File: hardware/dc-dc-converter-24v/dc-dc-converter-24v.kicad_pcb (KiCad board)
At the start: 4 copper layers, 100 x 100 mm, 56 parts, among them J1 12V, J2 24V, Q1 SQJA42EP, Q2 SQJA42EP, Q3 SQJA42EP, Q4 SQJA42EP, U1 LM5176

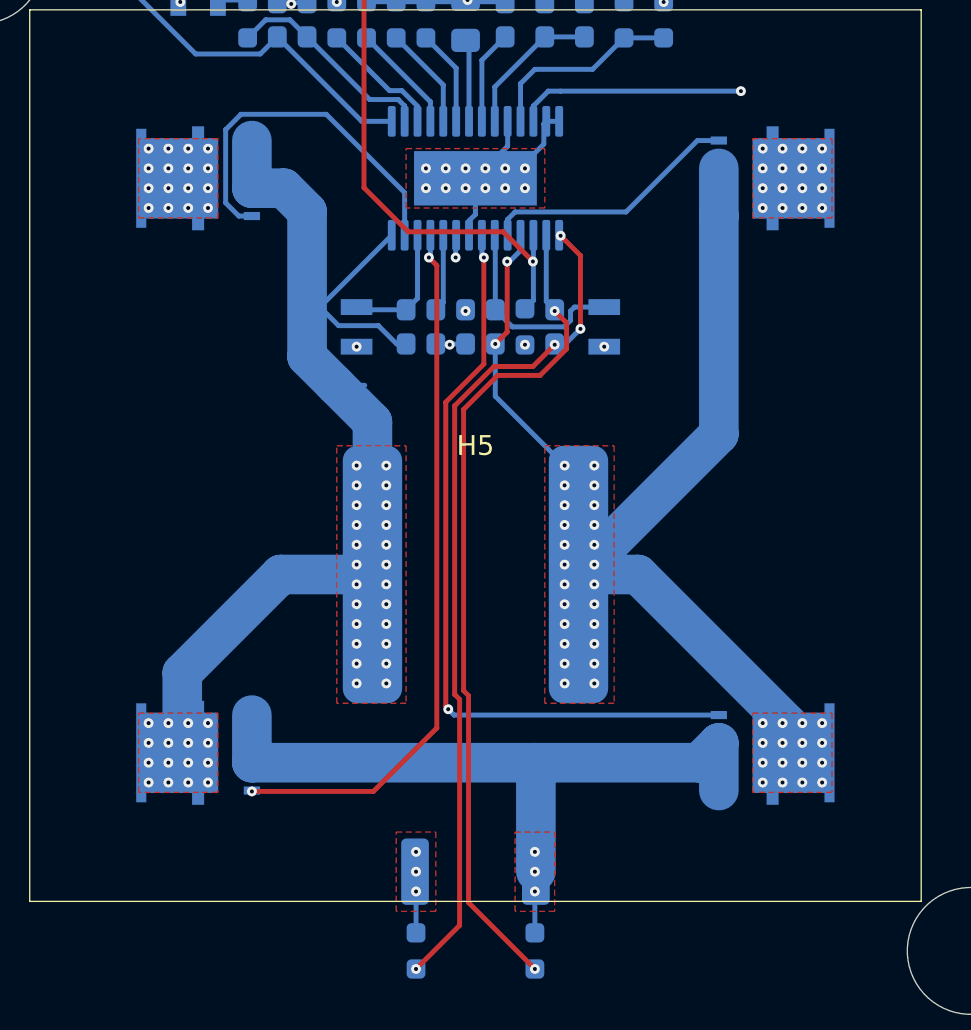
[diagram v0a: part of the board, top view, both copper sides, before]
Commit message: replace tracks in power path with zones
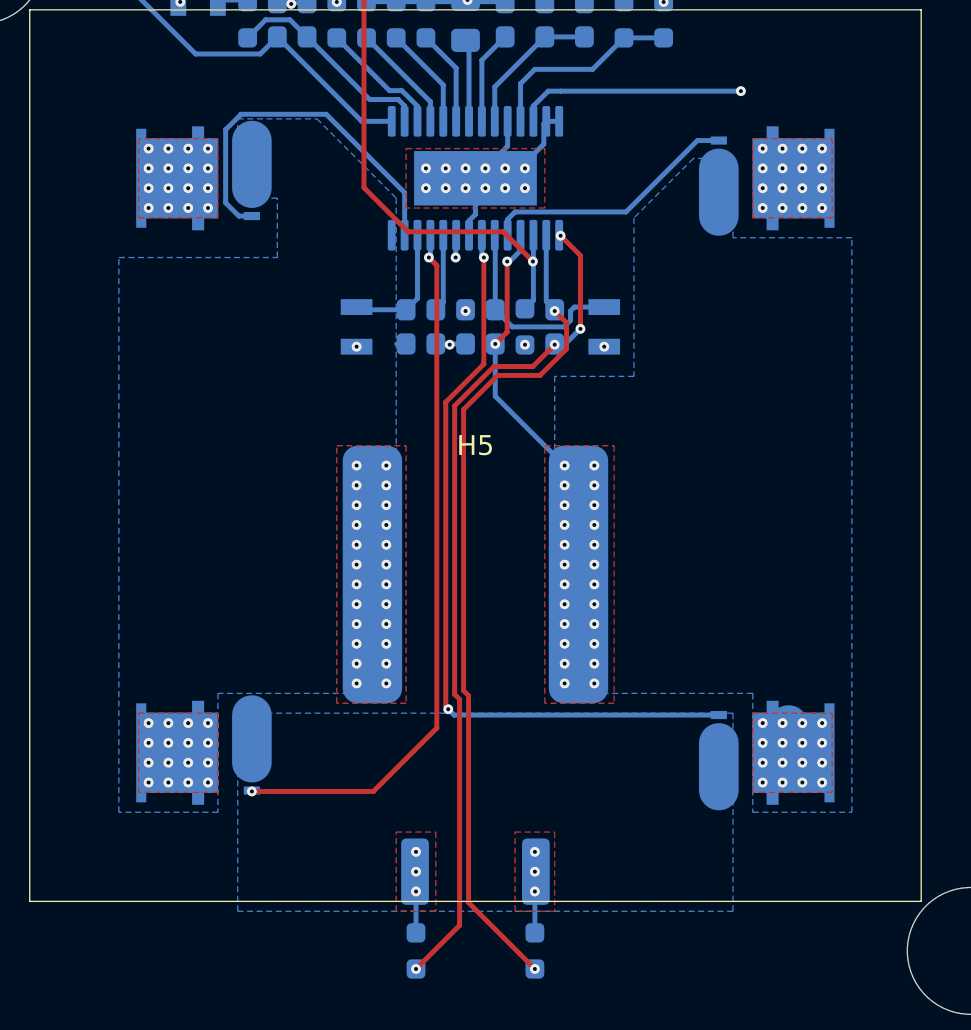
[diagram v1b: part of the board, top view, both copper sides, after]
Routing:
- net Net-(Q1-S): track 52.8 -> 2.88 mm
- net Net-(Q3-S): track 52.3 -> 17.5 mm
- net Net-(Q2-S): track 36.4 -> 6.90 mm
- added copper zone on B.Cu, net Net-(Q1-S)
- added copper zone on B.Cu, net Net-(Q2-S)
- added copper zone on B.Cu, net Net-(Q3-S)
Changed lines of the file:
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@@
-	)
-	(segment
-		(start 85.801 87.596)
-		(end 78.205 80)
-		(width 2)
-		(layer "B.Cu")
-		(net 11)
-	)
-	(segment
-		(start 82.285 72.915)
-		(end 75.2 80)
-		(width 2)
-		(layer "B.Cu")
-		(net 11)
-	)
-	(segment
-		(start 78.205 80)
-		(end 75.2 80)
-		(width 2)
-		(layer "B.Cu")
-		(net 11)
 	)
 	(segment
@@
 	)
 	(segment
-		(start 82.285 61.905)
-		(end 82.285 72.915)
-		(width 2)
-		(layer "B.Cu")
-		(net 11)
-	)
-	(segment
 		(start 85.801 89)
 		(end 85.801 87.596)
@@
 	)
 	(segment
-		(start 73.05 89.55)
-		(end 73.05 95)
-		(width 2)
-		(layer "B.Cu")
-		(net 21)
-	)
-	(segment
-		(start 58.715 89.5)
-		(end 73 89.5)
-		(width 2)
-		(layer "B.Cu")
-		(net 21)
-	)
-	(segment
 		(start 82.285 90.905)
 		(end 82.285 88.5)
@@
 	)
 	(segment
-		(start 81.285 89.5)
-		(end 82.285 88.5)
-		(width 2)
-		(layer "B.Cu")
-		(net 21)
-	)
-	(segment
 		(start 58.715 87.095)
 		(end 58.715 89.5)
@@
 		(net 21)
 	)
-	(segment
-		(start 73 89.5)
-		(end 73.05 89.55)
-		(width 2)
-		(layer "B.Cu")
-		(net 21)
-	)
-	(segment
-		(start 73 89.5)
-		(end 81.285 89.5)
-		(width 2)
-		(layer "B.Cu")
-		(net 21)
-	)
 	(via
 		(at 53.5 89.5)
@@
 		(drill 0.2)
 		(layers "F.Cu" "B.Cu")
-		(net 22)
-	)
-	(segment
-		(start 60.325 60.5)
-		(end 61.5 61.675)
-		(width 2)
-		(layer "B.Cu")
-		(net 22)
-	)
-	(segment
-		(start 64.4125 70.45)
-		(end 62.95 70.45)
-		(width 0.25)
-		(layer "B.Cu")
-		(net 22)
-	)
-	(segment
-		(start 63.0875 67.4375)
-		(end 62.15 66.5)
-		(width 0.25)
-		(layer "B.Cu")
-		(net 22)
-	)
-	(segment
-		(start 61.5 69)
-		(end 62.95 70.45)
-		(width 2)
-		(layer "B.Cu")
-		(net 22)
-	)
-	(segment
-		(start 58.715 60.5)
-		(end 60.325 60.5)
-		(width 2)
-		(layer "B.Cu")
-		(net 22)
-	)
-	(segment
-		(start 60.1685 80)
-		(end 64.8 80)
-		(width 2)
-		(layer "B.Cu")
-		(net 22)
-	)
-	(segment
-		(start 62.95 70.45)
-		(end 64.8 72.3)
-		(width 2)
-		(layer "B.Cu")
-		(net 22)
-	)
-	(segment
-		(start 61.5 61.675)
-		(end 61.5 69)
-		(width 2)
-		(layer "B.Cu")
-		(net 22)
-	)
-	(segment
-		(start 55.199 89)
-		(end 55.199 84.9695)
-		(width 2)
-		(layer "B.Cu")
-		(net 22)
-	)
-	(segment
-		(start 65.1 67.4375)
-		(end 63.0875 67.4375)
-		(width 0.25)
-		(layer "B.Cu")
 		(net 22)
 	)
@@
 		(end 66.025 68.3625)
 		(width 0.25)
-		(layer "B.Cu")
-		(net 22)
-	)
-	(segment
-		(start 55.199 84.9695)
-		(end 60.1685 80)
-		(width 2)
-		(layer "B.Cu")
-		(net 22)
-	)
-	(segment
-		(start 62.15 66.5)
-		(end 65.775 62.875)
-		(width 0.25)
-		(layer "B.Cu")
-		(net 22)
-	)
-	(segment
-		(start 66.025 68.3625)
-		(end 65.1 67.4375)
-		(width 0.25)
-		(layer "B.Cu")
-		(net 22)
-	)
-	(segment
-		(start 64.8 72.3)
-		(end 64.8 80)
-		(width 2)
 		(layer "B.Cu")
 		(net 22)
@@
 			)
 		)
+	)
+	(zone
+		(net 22)
+		(net_name "Net-(Q1-S)")
+		(layer "B.Cu")
+		(hatch edge 0.5)
+		(priority 13)
+		(connect_pads yes
+			(clearance 0.5)
+		)
+		(min_thickness 0.25)
+		(filled_areas_thickness no)
+		(fill yes
+			(thermal_gap 0.5)
+			(thermal_bridge_width 0.5)
+		)
+		(polygon
+			(pts
+				(xy 58 57) (xy 62 57) (xy 66 61) (xy 66 86) (xy 57 86) (xy 57 92) (xy 52 92) (xy 52 64) (xy 60 64)
+				(xy 60 61) (xy 58 61)
+			)
+		)
+	)
+	(zone
+		(net 11)
+		(net_name "Net-(Q3-S)")
+		(layer "B.Cu")
+		(hatch edge 0.5)
+		(priority 14)
+		(connect_pads yes
+			(clearance 0.5)
+		)
+		(min_thickness 0.25)
+		(filled_areas_thickness no)
+		(fill yes
+			(thermal_gap 0.5)
+			(thermal_bridge_width 0.5)
+		)
+		(polygon
+			(pts
+				(xy 83 59) (xy 81 59) (xy 78 62) (xy 78 70) (xy 74 70) (xy 74 86) (xy 84 86) (xy 84 92) (xy 89 92)
+				(xy 89 63) (xy 83 63)
+			)
+		)
+	)
+	(zone
+		(net 21)
+		(net_name "Net-(Q2-S)")
+		(layer "B.Cu")
+		(hatch edge 0.5)
+		(priority 15)
+		(connect_pads yes
+			(clearance 0.5)
+		)
+		(min_thickness 0.25)
+		(filled_areas_thickness no)
+		(fill yes
+			(thermal_gap 0.5)
+			(thermal_bridge_width 0.5)
+		)
+		(polygon
+			(pts
+				(xy 58 87) (xy 83 87) (xy 83 97) (xy 58 97)
+			)
+		)

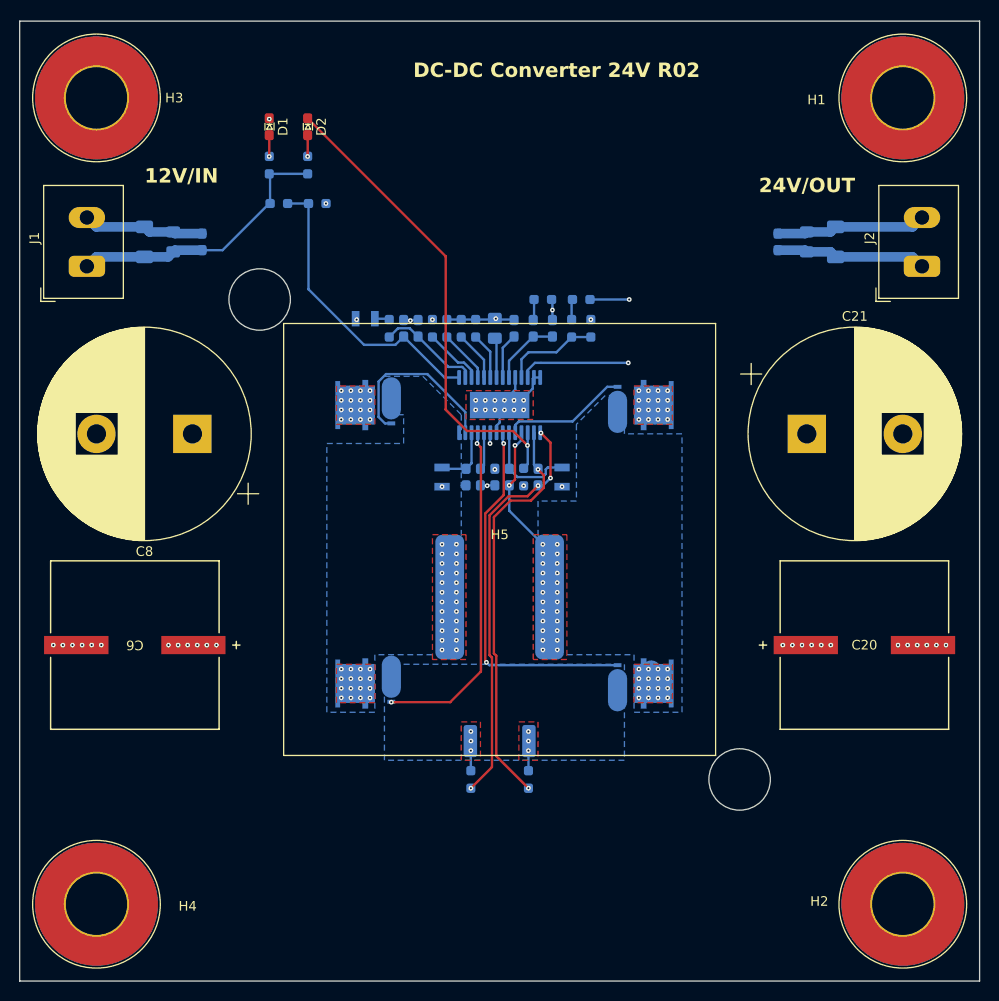
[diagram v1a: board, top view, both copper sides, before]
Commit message: improve layout of DC DC converter
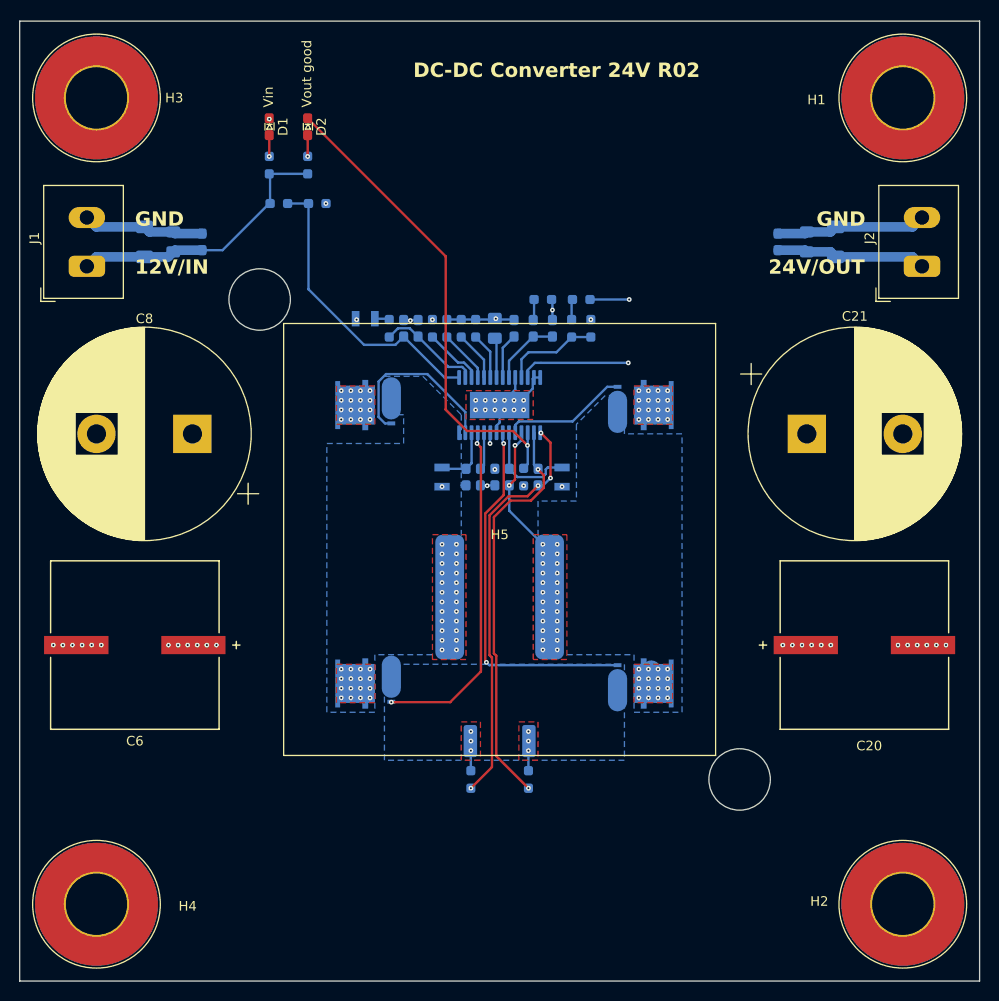
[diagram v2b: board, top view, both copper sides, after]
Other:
- board text added: "GND"
- board text added: "Vin"
- board text added: "Vout good"
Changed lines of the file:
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@@
 			(layer "F.SilkS")
 		)
+		(fp_circle
+			(center -25 -25)
+			(end -21 -22)
+			(stroke
+				(width 0.05)
+				(type default)
+			)
+			(fill none)
+			(layer "B.CrtYd")
+		)
+		(fp_circle
+			(center 25 25)
+			(end 29 27)
+			(stroke
+				(width 0.05)
+				(type default)
+			)
+			(fill none)
+			(layer "B.CrtYd")
+		)
 		(fp_line
 			(start -25 -32.5)
@@
 		(tags "CP Radial series Radial pin pitch 10.00mm  diameter 22mm Electrolytic Capacitor")
 		(property "Reference" "C8"
-			(at 5 -12.25 180)
+			(at 5 12 180)
 			(layer "F.SilkS")
 			(effects
@@
 		(tags "UCD1J471MNQ1MS ")
 		(property "Reference" "C20"
-			(at 0 0 0)
+			(at 0.5 10.5 0)
 			(unlocked yes)
 			(layer "F.SilkS")
@@
 			(pintype "passive")
 		)
+		(model "/home/benedikt/Development/electronics-library/3d-models/phoenix_1755736.stp"
+			(offset
+				(xyz -6.1 -3.9 0)
+			)
+			(scale
+				(xyz 1 1 1)
+			)
+			(rotate
+				(xyz 0 0 0)
+			)
+		)
 	)
 	(footprint "benediktibk:MountingHole_6.4mm_M6_Pad_TopBottom"
@@
 			(pintype "passive")
 		)
+		(model "/home/benedikt/Development/electronics-library/3d-models/phoenix_1755736.stp"
+			(offset
+				(xyz -6.1 -3.9 0)
+			)
+			(scale
+				(xyz 1 1 1)
+			)
+			(rotate
+				(xyz 0 0 0)
+			)
+		)
 	)
 	(footprint "benediktibk:MountingHole_6.4mm_M6_Pad_TopBottom"
@@
 		(tags "UCD1J471MNQ1MS ")
 		(property "Reference" "C6"
-			(at 0 0 180)
+			(at 0 -10 0)
 			(unlocked yes)
 			(layer "F.SilkS")
@@
 		(tags "MOSFET (N-Channel)")
 		(property "Reference" "Q1"
-			(at 0 0.001 90)
+			(at 0 4.5 90)
 			(layer "B.SilkS")
 			(effects
@@
 		(tags "capacitor handsolder")
 		(property "Reference" "C2"
-			(at 0 1.68 -90)
+			(at -4 0 -90)
 			(layer "B.SilkS")
 			(effects
@@
 		(tags "SOD-323")
 		(property "Reference" "D5"
-			(at 0 1.85 90)
+			(at 3.5 0 90)
 			(layer "B.SilkS")
 			(effects
@@
 		(tags "capacitor handsolder")
 		(property "Reference" "C7"
-			(at 0 1.43 -90)
+			(at 5 0 -90)
 			(layer "B.SilkS")
 			(effects
@@
 		(tags "resistor handsolder")
 		(property "Reference" "R12"
-			(at 0 1.43 -90)
+			(at -3.5 0 -90)
 			(layer "B.SilkS")
 			(effects
@@
 		(tags "SOD-323")
 		(property "Reference" "D3"
-			(at 0 1.85 180)
+			(at 0 4 -90)
 			(layer "B.SilkS")
 			(effects
@@
 		(tags "capacitor handsolder")
 		(property "Reference" "C1"
-			(at 0 1.43 -90)
+			(at -4 0 -90)
 			(layer "B.SilkS")
 			(effects
@@
 		(tags "capacitor handsolder")
 		(property "Reference" "C19"
-			(at 0 1.85 -90)
+			(at -4.5 0 -90)
 			(layer "B.SilkS")
 			(effects
@@
 		(tags "resistor handsolder")
 		(property "Reference" "R8"
-			(at 0 1.43 -90)
+			(at 5 0 -90)
 			(layer "B.SilkS")
 			(effects
@@
 		(tags "resistor handsolder")
 		(property "Reference" "R11"
-			(at 0 1.43 0)
+			(at 0 -1.5 0)
 			(layer "B.SilkS")
 			(effects
@@
 		(tags "resistor handsolder")
 		(property "Reference" "R14"
-			(at 0 1.43 90)
+			(at 3.5 0 90)
 			(layer "B.SilkS")
 			(effects
@@
 		(tags "Inductor")
 		(property "Reference" "L1"
-			(at 0 0 0)
+			(at -10 0 0)
 			(layer "B.SilkS")
 			(effects
@@
 		(sheetfile "dc-dc-converter-24v.kicad_sch")
 		(attr smd)
-		(fp_circle
-			(center -12.85 0)
-			(end -12.85 -0.05)
-			(stroke
-				(width 0.2)
-				(type solid)
-			)
-			(fill none)
-			(layer "B.SilkS")
-		)
 		(fp_line
 			(start -7 -7)
@@
 		(tags "MOSFET (N-Channel)")
 		(property "Reference" "Q2"
-			(at 0 0.001 90)
+			(at 0 4.5 90)
 			(layer "B.SilkS")
 			(effects
@@
 		(tags "MOSFET (N-Channel)")
 		(property "Reference" "Q4"
-			(at 0 0.001 -90)
+			(at 0 4.5 -90)
 			(layer "B.SilkS")
 			(effects
@@
 		(tags "capacitor handsolder")
 		(property "Reference" "C10"
-			(at 0 1.43 -90)
+			(at 4.5 0 -90)
 			(layer "B.SilkS")
 			(effects
@@
 		(tags "MOSFET (N-Channel)")
 		(property "Reference" "Q3"
-			(at 0 0.001 -90)
+			(at 0 4.5 -90)
 			(layer "B.SilkS")
 			(effects
@@
 		(tags "resistor handsolder")
 		(property "Reference" "R9"
-			(at 0 1.43 90)
+			(at -5 0 90)
 			(layer "B.SilkS")
 			(effects
@@
 		(tags "resistor handsolder")
 		(property "Reference" "R3"
-			(at 0 1.43 -90)
+			(at -3.5 0 -90)
 			(layer "B.SilkS")
 			(effects
@@
 		(tags "capacitor handsolder")
 		(property "Reference" "C15"
-			(at 0 1.43 90)
+			(at 4 0 90)
 			(layer "B.SilkS")
 			(effects
@@
 		(tags "capacitor handsolder")
 		(property "Reference" "C9"
-			(at 0 1.43 90)
+			(at 3.5 0 90)
 			(layer "B.SilkS")
 			(effects
@@
 		(tags "capacitor handsolder")
 		(property "Reference" "C3"
-			(at 0 1.43 90)
+			(at 3.5 0 90)
 			(layer "B.SilkS")
 			(effects
@@
 		(tags "capacitor handsolder")
 		(property "Reference" "C17"
-			(at 0 1.43 -90)
+			(at -4.5 0 -90)
 			(layer "B.SilkS")
 			(effects
@@
 		(tags "SOD-323")
 		(property "Reference" "D4"
-			(at 0 1.85 90)
+			(at 3.5 0 90)
 			(layer "B.SilkS")
 			(effects
@@
 		(tags "capacitor handsolder")
 		(property "Reference" "C14"
-			(at 0 1.43 90)
+			(at 4 0 90)
 			(layer "B.SilkS")
 			(effects
@@
 		(tags "capacitor handsolder")
 		(property "Reference" "C16"
-			(at 0 1.43 90)
+			(at 4 0 90)
 			(layer "B.SilkS")
 			(effects
@@
 		(tags "capacitor handsolder")
 		(property "Reference" "C11"
-			(at 0 1.43 -90)
+			(at -3.5 0 -90)
 			(layer "B.SilkS")
 			(effects
@@
 		(tags "resistor handsolder")
 		(property "Reference" "R10"
-			(at 0 1.43 90)
+			(at -4.5 0 90)
 			(layer "B.SilkS")
 			(effects
@@
 		(tags "capacitor handsolder")
 		(property "Reference" "C18"
-			(at 0 1.68 -90)
+			(at -4.5 0 -90)
 			(layer "B.SilkS")
 			(effects
@@
 		(tags "capacitor handsolder")
 		(property "Reference" "C4"
-			(at 0 1.85 -90)
+			(at -4 0 -90)
 			(layer "B.SilkS")
 			(effects
@@
 		(tags "capacitor handsolder")
 		(property "Reference" "C5"
-			(at 0 1.43 -90)
+			(at 5 0 -90)
 			(layer "B.SilkS")
 			(effects
@@
 		(tags "resistor handsolder")
 		(property "Reference" "R5"
-			(at 0 1.43 90)
+			(at -5 0 90)
 			(layer "B.SilkS")
 			(effects
@@
 		(tags "resistor handsolder")
 		(property "Reference" "R4"
-			(at 0 1.43 -90)
+			(at 5 0 -90)
 			(layer "B.SilkS")
 			(effects
@@
 		(tags "capacitor handsolder")
 		(property "Reference" "C12"
-			(at 0 1.68 -90)
+			(at 4.5 0 -90)
 			(layer "B.SilkS")
 			(effects
@@
 		(tags "capacitor handsolder")
 		(property "Reference" "C13"
-			(at 0 1.43 -90)
+			(at -3 0 -90)
 			(layer "B.SilkS")
 			(effects
@@
 		(layer "Edge.Cuts")
 	)
+	(gr_text "GND"
+		(at 103 41.5 0)
+		(layer "F.SilkS")
+		(effects
+			(font
+				(size 1.5 1.5)
+				(thickness 0.3)
+				(bold yes)
+			)
+			(justify left bottom)
+		)
+	)
+	(gr_text "GND"
+		(at 32 41.5 0)
+		(layer "F.SilkS")
+		(effects
+			(font
+				(size 1.5 1.5)
+				(thickness 0.3)
+				(bold yes)
+			)
+			(justify left bottom)
+		)
+	)
 	(gr_text "DC-DC Converter 24V R02"
 		(at 61 26 0)
@@
 		)
 	)
+	(gr_text "Vout good"
+		(at 50.5 29 90)
+		(layer "F.SilkS")
+		(effects
+			(font
+				(size 1 1)
+				(thickness 0.15)
+			)
+			(justify left bottom)
+		)
+	)
+	(gr_text "Vin"
+		(at 46.5 29 90)
+		(layer "F.SilkS")
+		(effects
+			(font
+				(size 1 1)
+				(thickness 0.15)
+			)
+			(justify left bottom)
+		)
+	)
 	(gr_text "24V/OUT"
-		(at 97 38 0)
+		(at 98 46.5 0)
 		(layer "F.SilkS")
 		(effects
@@
 	)
 	(gr_text "12V/IN"
-		(at 33 37 0)
+		(at 32 46.5 0)
 		(layer "F.SilkS")
 		(effects
@@
 		(width 0.25)
 		(layer "F.Cu")
-		(net 18)
-	)
-	(segment
-		(start 64.4 44.525)
-		(end 64.375 44.5)
-		(width 0.25)
-		(layer "F.Cu")
